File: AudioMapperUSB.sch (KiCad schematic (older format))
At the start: 153 parts, among them J1 USB_B, J10 Conn_01x01, J11 Conn_01x01, J12 Conn_Coaxial, J13 Conn_Coaxial, J14 Conn_Coaxial, J15 Conn_Coaxial, J16 Audio-Jack-2, J17 Audio-Jack-2, J18 Audio-Jack-2, J19 Audio-Jack-2, J2 Audio-Jack-2, J20 Audio-Jack-2, J21 Audio-Jack-2, J3 Conn_01x02, J4 Audio-Jack-2, J5 Conn_01x02, J6 Conn_01x02, J7 Conn_01x02, J8 Conn_01x01, J9 Conn_01x01, Q1 SS8550, Q2 MMBT3904, Q3 MMBT3904, U1 AMS1117-3.3, U2 PCM2900, U3 OPA2170, U4 OPA2170, U5 OPA2170, U6 OPA2170, Y1 12 MHz

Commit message: Fixed backward polarity audio connectors.  Duh.
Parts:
- R63, R64: value 10k -> 1k; LCSC C17414 -> C17513
- R65: value 2k2 -> 10k; LCSC C17520 -> C17414
- R66: value 10k -> 100k; LCSC C17414 -> C17407
- R67: value 220R -> 100R; LCSC 220R -> C17408
- R68: value 100R -> NC; LCSC C17408 -> (none)
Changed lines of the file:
@@
 P 7550 1100
 F 0 "R67" V 7450 1100 50  0000 C CNN
-F 1 "220R" V 7550 1100 50  0000 C CNN
+F 1 "100R" V 7550 1100 50  0000 C CNN
 F 2 "Resistors_SMD:R_0805_HandSoldering" V 7480 1100 50  0001 C CNN
 F 3 "" H 7550 1100 50  0001 C CNN
-F 4 "220R" V 7550 1100 60  0001 C CNN "LCSC"
+F 4 " C17408" V 7550 1100 60  0001 C CNN "LCSC"
 	1    7550 1100
 	1    0    0    -1
@@
 P 7300 1150
 F 0 "R66" V 7380 1150 50  0000 C CNN
-F 1 "10k" V 7300 1150 50  0000 C CNN
+F 1 "100k" V 7300 1150 50  0000 C CNN
 F 2 "Resistors_SMD:R_0805_HandSoldering" V 7230 1150 50  0001 C CNN
 F 3 "" H 7300 1150 50  0001 C CNN
-F 4 "C17414" V 7300 1150 60  0001 C CNN "LCSC"
+F 4 " C17407" V 7300 1150 60  0001 C CNN "LCSC"
 	1    7300 1150
 	-1   0    0    -1
@@
 P 7200 1600
 F 0 "R65" V 7280 1600 50  0000 C CNN
-F 1 "2k2" V 7200 1600 50  0000 C CNN
+F 1 "10k" V 7200 1600 50  0000 C CNN
 F 2 "Resistors_SMD:R_0805_HandSoldering" V 7130 1600 50  0001 C CNN
 F 3 "" H 7200 1600 50  0001 C CNN
-F 4 "C17520" V 7200 1600 60  0001 C CNN "LCSC"
+F 4 "C17414" V 7200 1600 60  0001 C CNN "LCSC"
 	1    7200 1600
 	0    1    1    0
@@
 P 6950 1000
 F 0 "R64" V 7030 1000 50  0000 C CNN
-F 1 "10k" V 6950 1000 50  0000 C CNN
+F 1 "1k" V 6950 1000 50  0000 C CNN
 F 2 "Resistors_SMD:R_0805_HandSoldering" V 6880 1000 50  0001 C CNN
 F 3 "" H 6950 1000 50  0001 C CNN
-F 4 "C17414" V 6950 1000 60  0001 C CNN "LCSC"
+F 4 "C17513" V 6950 1000 60  0001 C CNN "LCSC"
 	1    6950 1000
 	-1   0    0    -1
@@
 P 6500 1000
 F 0 "R63" V 6580 1000 50  0000 C CNN
-F 1 "10k" V 6500 1000 50  0000 C CNN
+F 1 "1k" V 6500 1000 50  0000 C CNN
 F 2 "Resistors_SMD:R_0805_HandSoldering" V 6430 1000 50  0001 C CNN
 F 3 "" H 6500 1000 50  0001 C CNN
-F 4 "C17414" V 6500 1000 60  0001 C CNN "LCSC"
+F 4 "C17513" V 6500 1000 60  0001 C CNN "LCSC"
 	1    6500 1000
 	1    0    0    -1
@@
 P 7550 750
 F 0 "R68" V 7450 750 50  0000 C CNN
-F 1 "100R" V 7550 750 50  0000 C CNN
+F 1 "NC" V 7550 750 50  0000 C CNN
 F 2 "Resistors_SMD:R_0805_HandSoldering" V 7480 750 50  0001 C CNN
 F 3 "" H 7550 750 50  0001 C CNN
-F 4 " C17408" V 7550 750 60  0001 C CNN "LCSC"
 	1    7550 750
 	0    -1   -1   0

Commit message: Added external power
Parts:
- removed J12, J13, J14, J15: Conn_Coaxial, Connectors:SMA_THT_Jack_Straight, symbol Conn_Coaxial
- added C45, C46: 1000 uF, Capacitors_THT:CP_Radial_D10.0mm_P5.00mm, symbol CP_Small
- added C47: 1 uF, Capacitors_SMD:C_0805_HandSoldering, symbol C_Small
- added J12: Jack-DC, Connectors:BARREL_JACK, symbol Jack-DC
- added JP8: Jumper_NC_Dual, Pin_Headers:Pin_Header_Straight_1x03_Pitch2.54mm, symbol Jumper_NC_Dual
- added U7: KA78M05_TO252, TO_SOT_Packages_SMD:TO-252-3_TabPin2, symbol KA78M05_TO252
- R52, R54: value 100k -> 22k; LCSC C17407 -> C17560
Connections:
- net GND: now also C45.2, C46.2, C47.1, J12.2, U7.2 (GND)
- net at C1.1, C19.1, C20.2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: now also C45.1, C46.1, JP8.2; no longer J1.1 (VBUS)
- new net: J1.1 (VBUS), JP8.1
- new net: C47.2, J12.1, U7.1 (VI)
- new net: JP8.3, U7.3 (VO)
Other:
- moved on the sheet: J1, R1

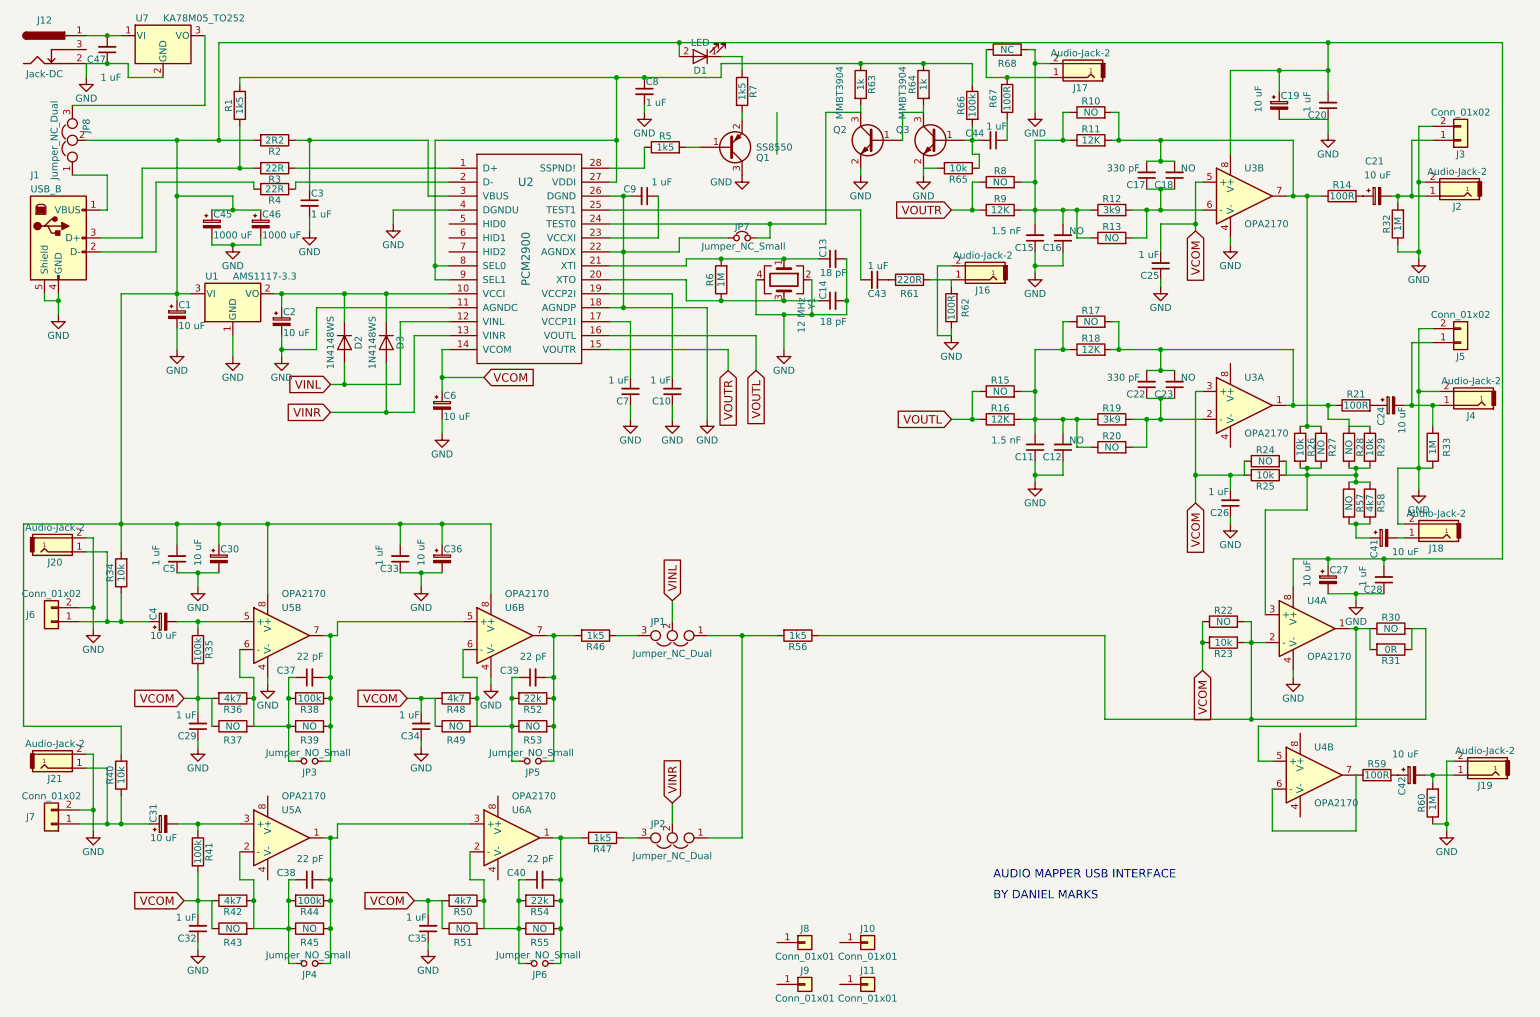
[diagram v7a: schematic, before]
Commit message: Use inverter for SPDIF
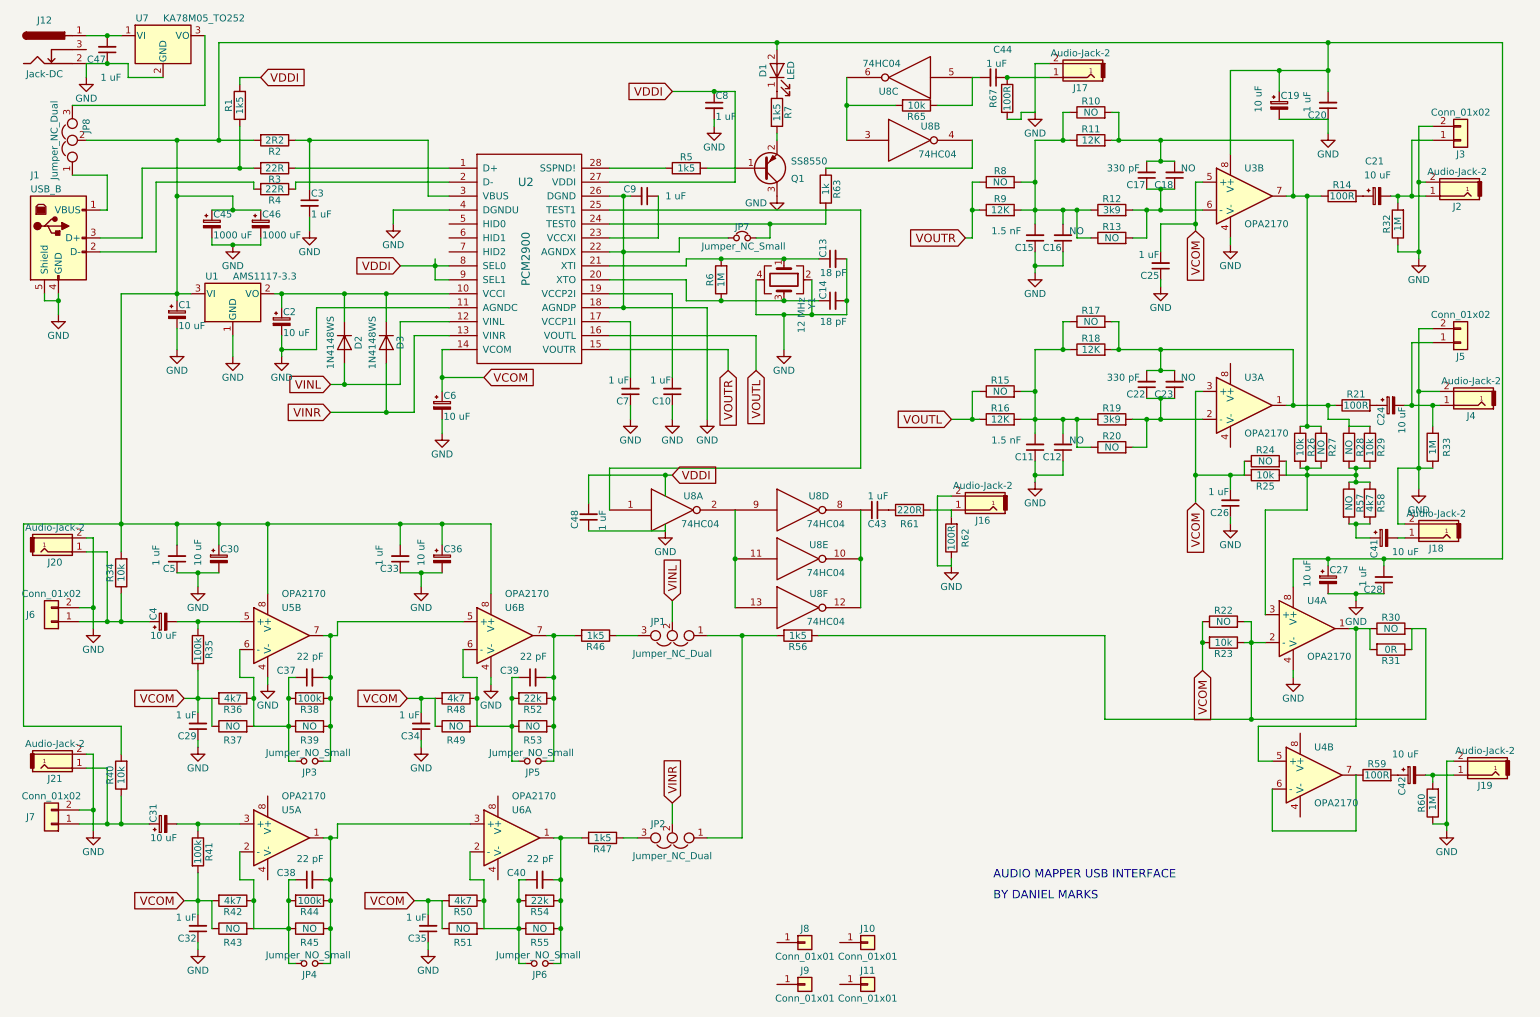
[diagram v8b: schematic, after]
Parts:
- removed Q2, Q3: MMBT3904, TO_SOT_Packages_SMD:SOT-23, symbol MMBT3904
- removed R64: 1k, Resistors_SMD:R_0805_HandSoldering, symbol R
- removed R66: 100k, Resistors_SMD:R_0805_HandSoldering, symbol R
- removed R68: NC, Resistors_SMD:R_0805_HandSoldering, symbol R
- added C48: 1 uF, Capacitors_SMD:C_0805_HandSoldering, symbol C_Small
- added U8: 74HC04, Housings_SOIC:SOIC-14_3.9x8.7mm_Pitch1.27mm, symbol 74HC04
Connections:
- net GND: now also R67.2, C48.1, U8.7 (GND), U8.7 (GND), U8.7 (GND), U8.7 (GND), U8.7 (GND), U8.7 (GND); no longer R65.2
- net at U2.25 (TEST1): now also U8.1; no longer C43.2
- net VCC: now reaches C8.1, R1.2, U2.27 (VDDI), U2.8 (SEL0), U2.9 (SEL1)
- net VCC: now also C48.2, U8.14 (VCC), U8.14 (VCC), U8.14 (VCC), U8.14 (VCC), U8.14 (VCC), U8.14 (VCC); no longer R63.1
- net at J17.1, R67.1: now also C44.1
- net at C44.2, R65.1: now also U8.5
- new net: C43.2, U8.10, U8.12, U8.8
- new net: R63.1, U8.4
- new net: U8.11, U8.13, U8.2, U8.9
- new net: R65.2, U8.3, U8.6
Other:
- moved on the sheet: C43, C44, C8, D1, J16, Q1, R5, R61, R62, R63, R7
